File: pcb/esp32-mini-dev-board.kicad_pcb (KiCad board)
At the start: 4 copper layers, 31 x 37.9 mm, 32 parts, among them J1 USB_C_Receptacle_USB2.0_16P, J2 Conn_01x08_Pin, J3 Conn_01x08_Pin, SW1 SW_Push, SW2 SW_Push, U1 USBLC6-2SC6, U2 AP2112K-3.3, U3 ESP32-C3-WROOM-02, Y1 Crystal

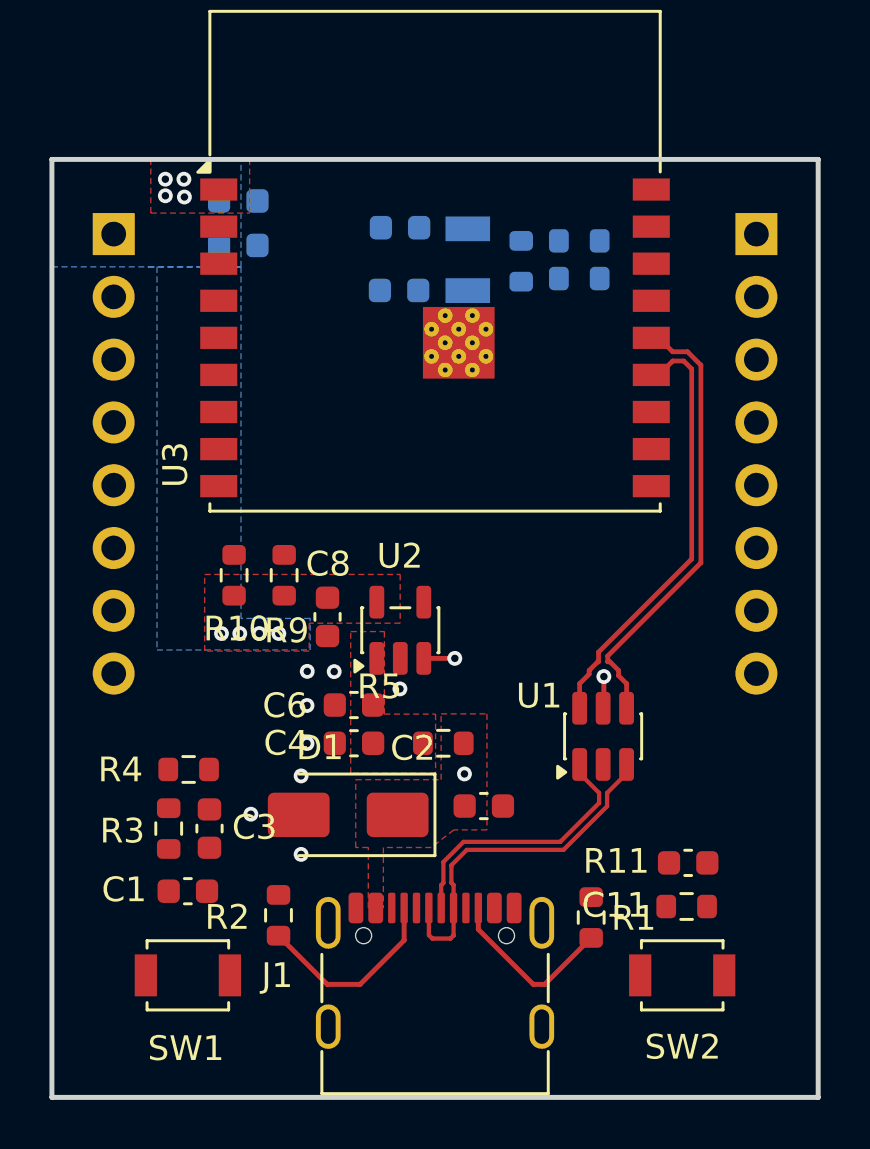
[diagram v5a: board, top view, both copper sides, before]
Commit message: feat(lay/osc): add xtal oscillator circuit
The USB differential pair was redrawn to ensure symmetrical traces length.
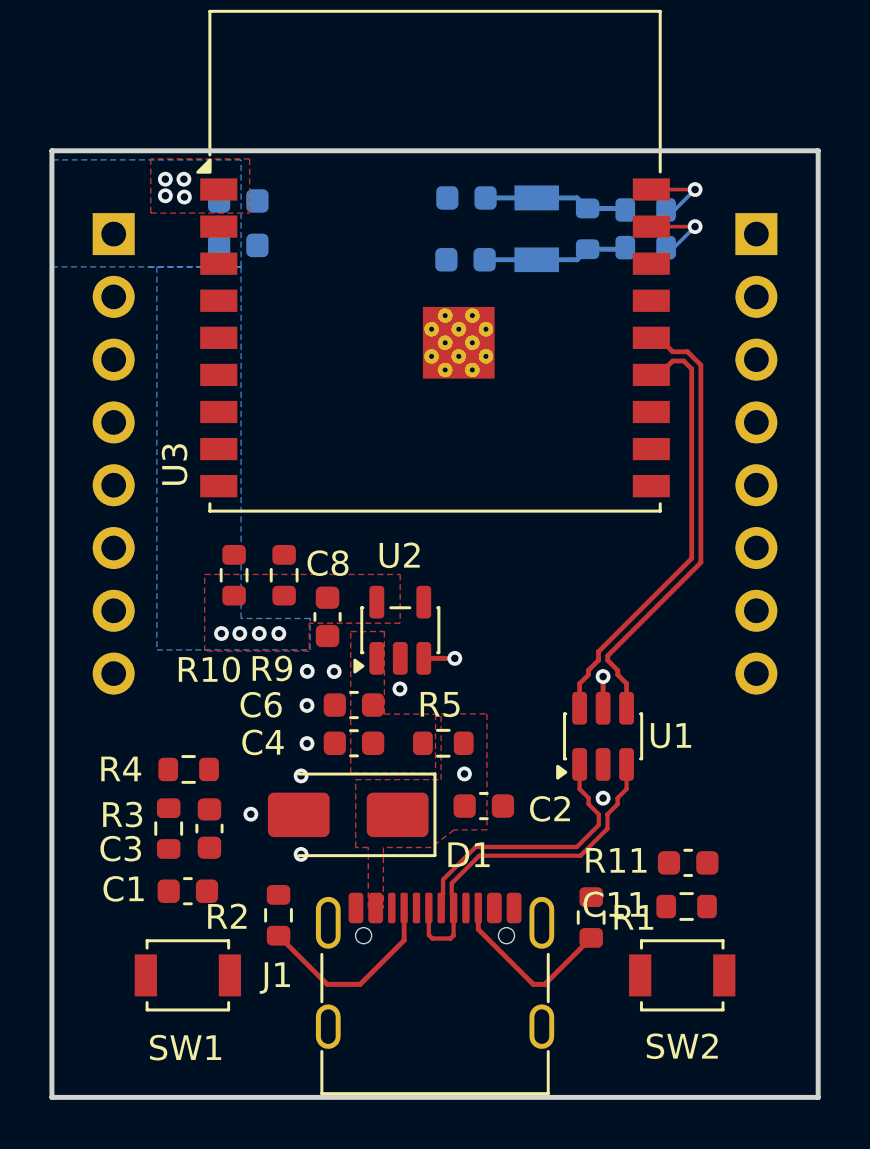
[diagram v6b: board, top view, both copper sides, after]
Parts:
- moved Y1 3.05 mm to (167.1, 99.8)
- moved R7 2.99 mm to (169.2, 99.8)
- moved R6 2.96 mm to (171.5, 99.0)
- moved R8 2.96 mm to (171.5, 100.5)
- moved C7 2.96 mm to (164.2, 101.0)
- moved C5 2.94 mm to (164.3, 98.5)
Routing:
- net Net-(C7-Pad1): track 0.00 -> 5.89 mm
- net Net-(C5-Pad1): track 0.00 -> 5.85 mm
- net /CIRCUIT DESIGN/XTAL_32K_N: track 0.00 -> 3.30 mm, vias 0 -> 1
- net /CIRCUIT DESIGN/XTAL_32K_P: track 0.00 -> 3.29 mm, vias 0 -> 1
- net GND: vias 8 -> 9
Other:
- board size 31 x 37.9 mm -> 31 x 38.3 mm

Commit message: feat(lay): finish routing and copper pouring
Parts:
- J1: footprint Connector_USB:USB_C_Receptacle_G-Switch_GT-USB-7010ASV -> CONNECTORS:USB_C_Receptacle_G-Switch_GT-USB-7010ASV
- moved C1 21.9 mm to (174.9, 127.4)
- moved C3 21.9 mm to (175.8, 124.9)
- moved R3 21.9 mm to (174.1, 124.9)
- moved R4 21.9 mm to (174.9, 122.5)
- moved SW1 21.9 mm to (174.9, 130.8)
- moved R11 20.3 mm to (152.9, 127.3)
- moved SW2 20.3 mm to (152.7, 130.1)
- moved C11 20.3 mm to (152.9, 125.6)
- moved C5 4.00 mm to (160.3, 98.5)
- moved C7 4.00 mm to (160.2, 101.0)
- moved R6 4.00 mm to (167.5, 99.0)
- moved R7 4.00 mm to (165.2, 99.8)
- moved R8 4.00 mm to (167.5, 100.5)
- moved Y1 4.00 mm to (163.1, 99.8)
- moved C2 1.28 mm to (166.2, 123.2)
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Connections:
- C3 pad 1: /CIRCUIT DESIGN/EN_RST -> /CIRCUIT DESIGN/EN
- R3 pad 2: /CIRCUIT DESIGN/EN_RST -> /CIRCUIT DESIGN/EN
- R4 pad 2: /CIRCUIT DESIGN/EN_RST -> /CIRCUIT DESIGN/EN
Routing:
- net /CIRCUIT DESIGN/EN: track 0.00 -> 45.4 mm, vias 0 -> 1
- net +3V3: track 0.00 -> 37.0 mm, vias 8 -> 10
- net /CIRCUIT DESIGN/BOOT: track 0.00 -> 25.7 mm
- net Net-(U3-IO2): track 0.00 -> 23.8 mm
- net /CIRCUIT DESIGN/IO10: track 0.00 -> 12.1 mm, vias 0 -> 1
- net /CIRCUIT DESIGN/IO7: track 0.00 -> 11.9 mm
- net /CIRCUIT DESIGN/IO6: track 0.00 -> 11.0 mm
- net /CIRCUIT DESIGN/IO5: track 0.00 -> 9.91 mm
- net GND: track 0.00 -> 9.36 mm, vias 9 -> 17
- net /CIRCUIT DESIGN/IO4: track 0.00 -> 8.91 mm
- net /CIRCUIT DESIGN/RXD: track 0.00 -> 8.71 mm, vias 0 -> 1
- net /CIRCUIT DESIGN/TXD: track 0.00 -> 8.26 mm, vias 0 -> 1
- net Net-(U3-IO8): track 0.00 -> 7.75 mm
- net Net-(C1-Pad1): track 0.00 -> 5.79 mm
- net /CIRCUIT DESIGN/IO3: track 0.00 -> 5.24 mm
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- added copper zone on In2.Cu, net +3V3
- added copper zone on In2.Cu, net +5V
- added copper zone on In2.Cu, net /CIRCUIT DESIGN/VBUS
- added copper zone on F.Cu, net GND
- added copper zone on In1.Cu, net GND
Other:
- board size 31 x 38.3 mm -> 31 x 37.8 mm

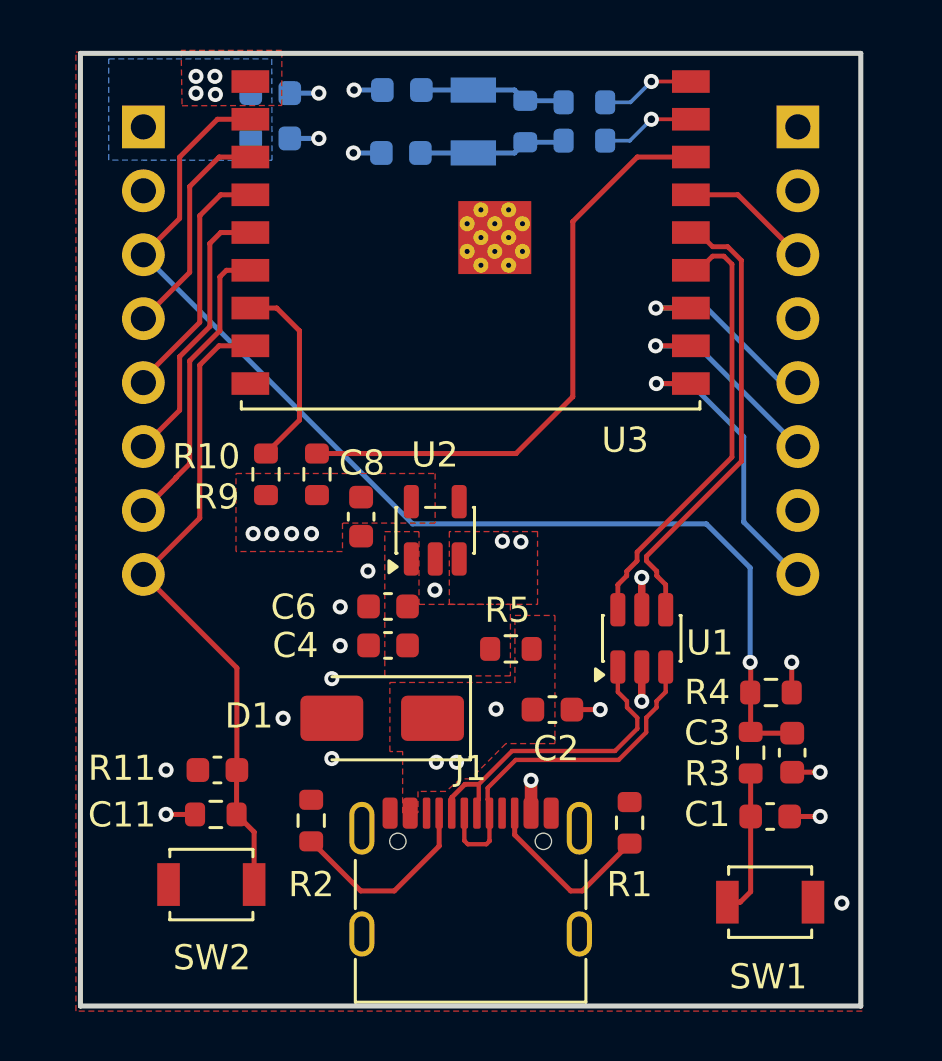
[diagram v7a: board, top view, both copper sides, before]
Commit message: feat(lay): add silkscreen labels for IOs and power pins
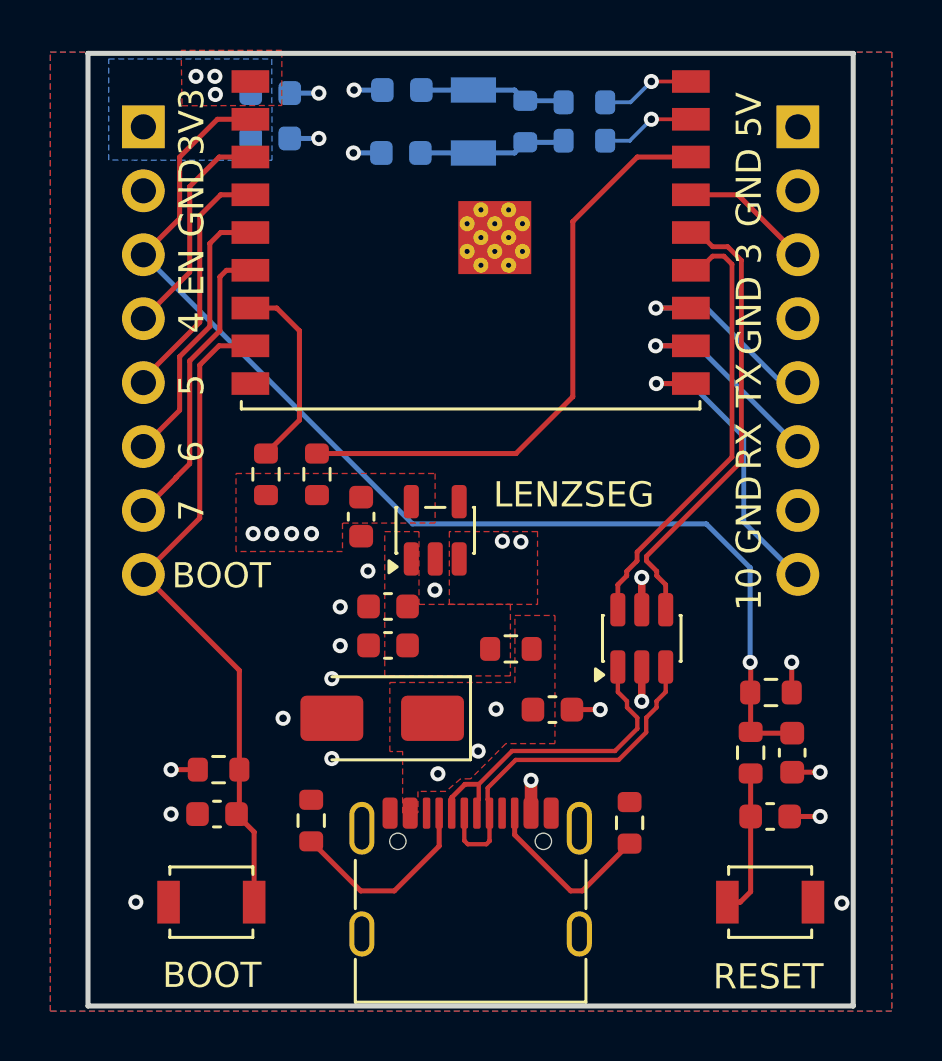
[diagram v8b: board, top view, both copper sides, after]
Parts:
- moved R11 1.78 mm to (153.0, 125.5)
- moved C11 1.75 mm to (152.9, 127.3)
- moved BOOT 0.70 mm to (152.7, 130.8)
- renumbered SW2 to BOOT, SW1 to RESET
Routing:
- net +3V3: track 37.0 -> 34.4 mm, vias 10 -> 9
- net /CIRCUIT DESIGN/BOOT: track 25.7 -> 26.5 mm
- net GND: vias 17 -> 18
- added copper zone on B.Cu, net GND
- added copper zone on In2.Cu, net GND
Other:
- board size 31 x 37.8 mm -> 30.4 x 37.8 mm
- board text added: "10"
- board text added: "3"
- board text added: "3V3"
- board text added: "4"
- board text added: "5"
- board text added: "5V"
- board text added: "6"
- board text added: "7"
- board text added: "BOOT"
- board text added: "EN"
- board text added: "GND"
- board text added: "LENZSEG"
- board text added: "RX"
- board text added: "TX"
